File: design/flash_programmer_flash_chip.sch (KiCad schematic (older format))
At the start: 7 parts, among them U401 GLS27SF010

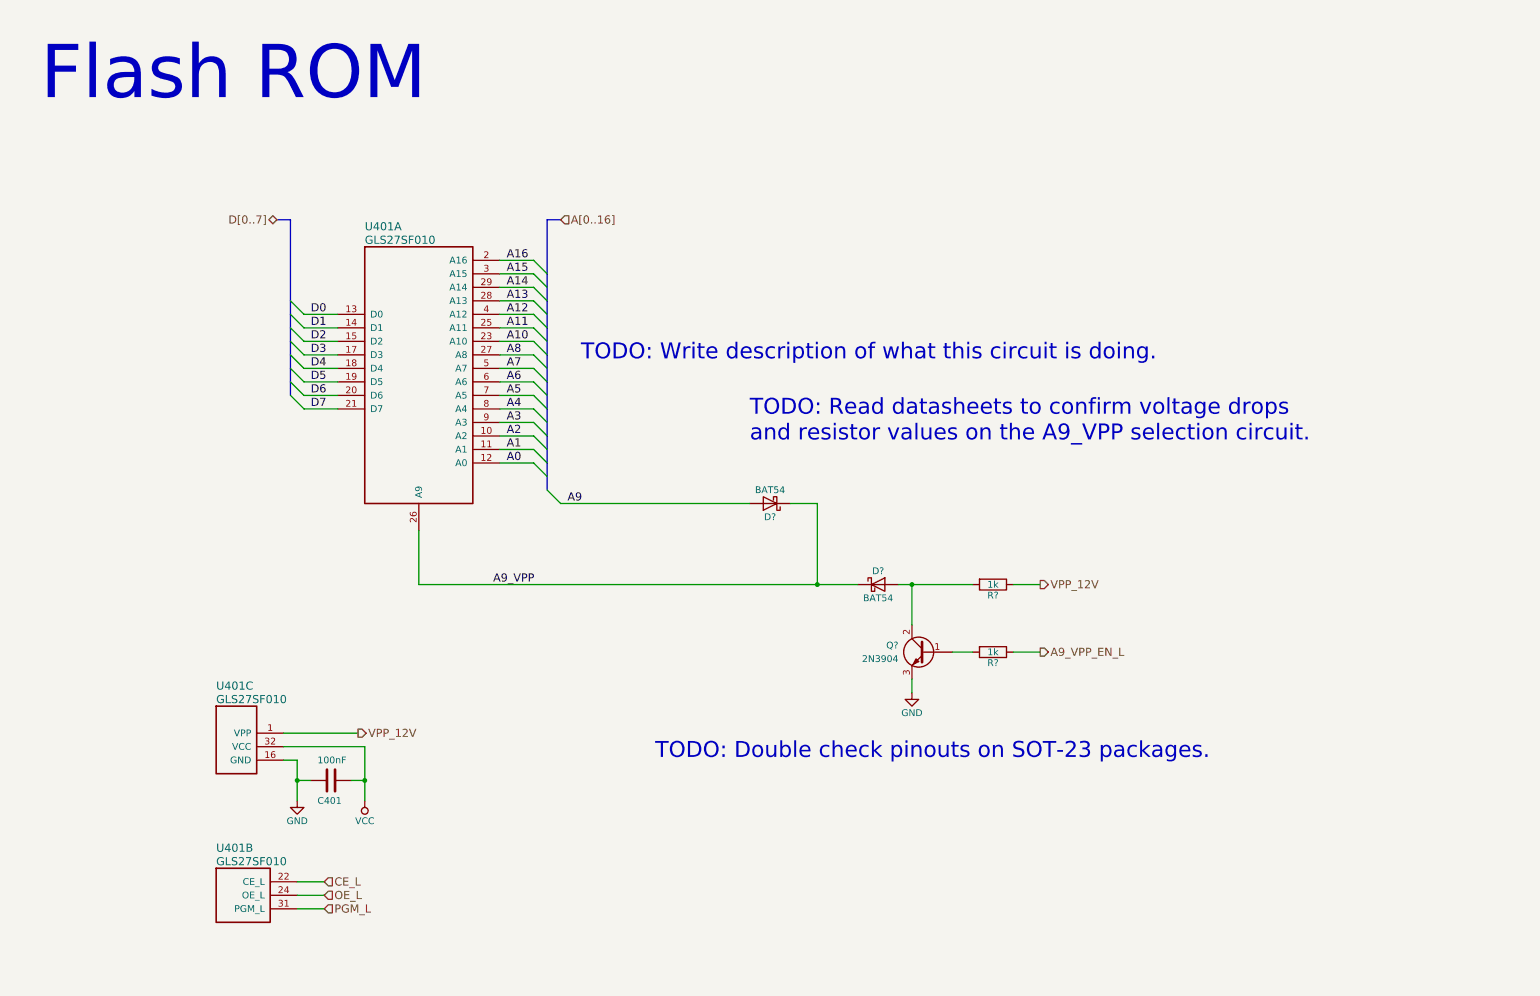
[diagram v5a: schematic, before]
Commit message: More schematic clean up
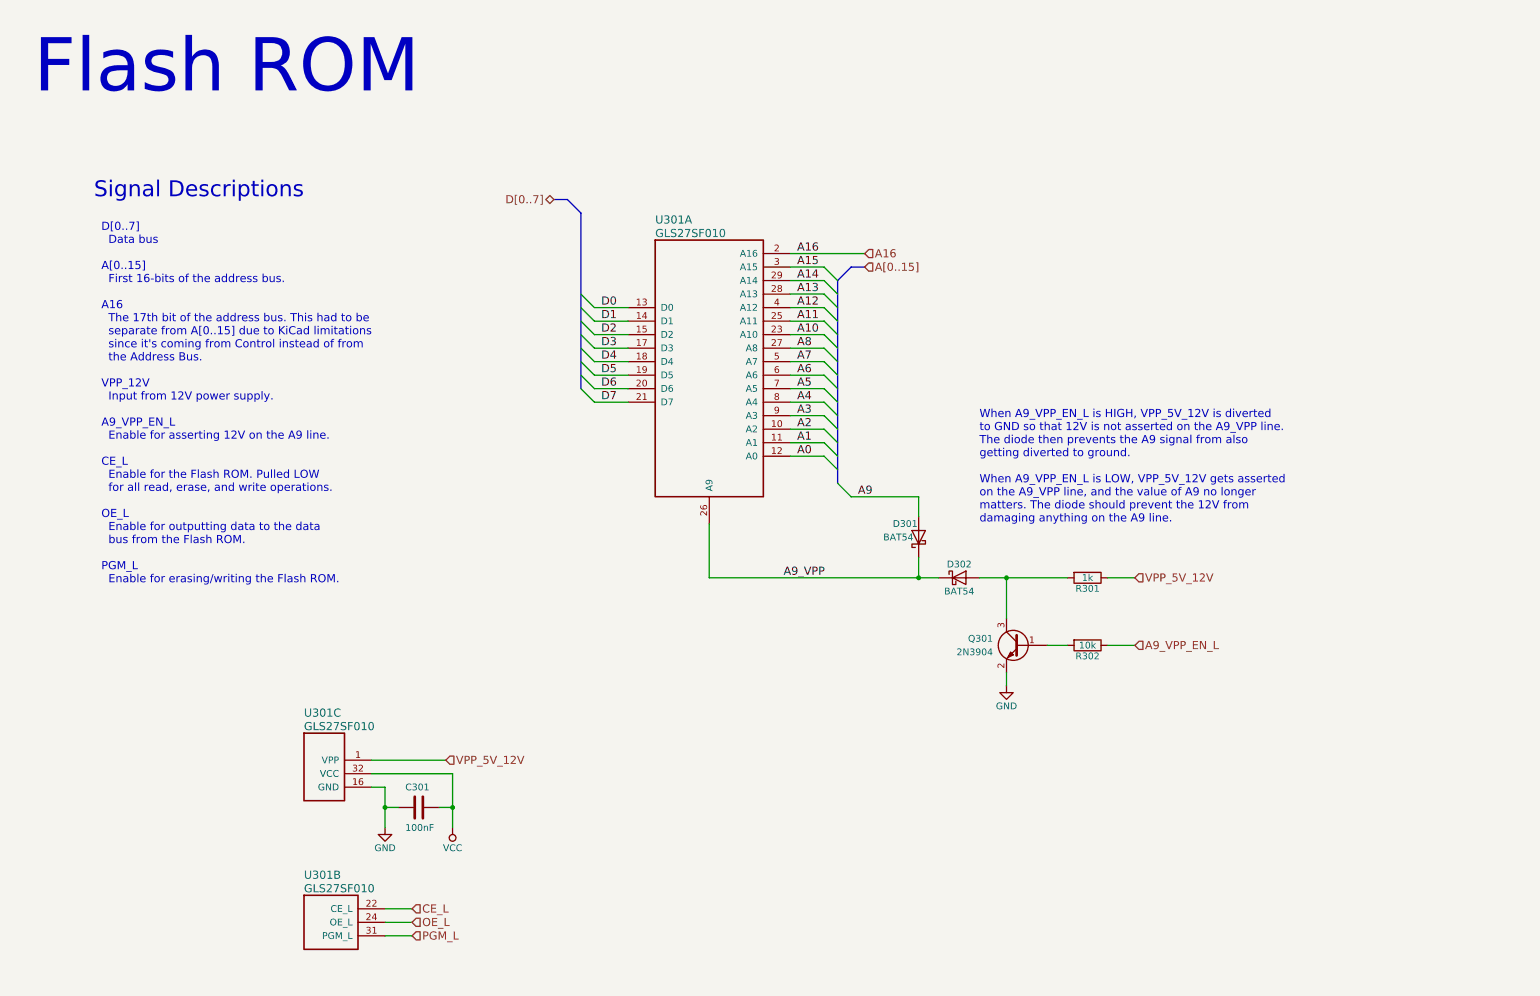
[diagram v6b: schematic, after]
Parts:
- removed Q?: 2N3904, symbol Q_NPN_BCE
- added Q301: 2N3904, TO_SOT_Packages_SMD:SOT-23_Handsoldering, symbol Q_NPN_BEC
- C301: renamed from C401; footprint Resistors_SMD:R_0805_HandSoldering -> Resistors_SMD:R_0603_HandSoldering
- D301, D302: renamed from D?; footprint (none) -> Diodes_SMD:D_SOT-23_ANK
- R301: renamed from R?; footprint (none) -> Resistors_SMD:R_0603_HandSoldering
- R302: renamed from R?; value 1k -> 10k; footprint (none) -> Resistors_SMD:R_0603_HandSoldering
- renumbered U401 to U301
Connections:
- net GND: now also Q301.2 (E)
- net at R302.2: now also Q301.1 (B)
- net at D302.2 (A), R301.2: now also Q301.3 (C)
- net VPP_12V renamed VPP_5V_12V
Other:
- note added: "D[0..7]\n Data bus\n\nA[0..15]\n First 16-bits of the address bus.\n\nA16\n The 17th bit of the address bus. This had to be\n separate from A[0..15] due to KiCad limitations\n since it's coming from Control instead of from\n the Address Bus.\n\nVPP_12V\n Input from 12V power supply.\n\nA9_VPP_EN_L\n Enable for asserting 12V on the A9 line.\n\nCE_L\n Enable for the Flash ROM. Pulled LOW\n for all 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"
- note added: "Signal Descriptions"
- note added: "When A9_VPP_EN_L is HIGH, VPP_5V_12V is diverted\nto GND so that 12V is not asserted on the A9_VPP line.\nThe diode then prevents the A9 signal from also\ngetting diverted to ground.\n\nWhen A9_VPP_EN_L is LOW, VPP_5V_12V gets asserted\non the A9_VPP line, and the value of A9 no longer\nmatters. The diode should prevent the 12V from\ndamaging anything on the A9 line."
- note removed: "TODO: Double check pinouts on SOT-23 packages."
- note removed: "TODO: Read datasheets to confirm voltage drops\nand resistor values on the A9_VPP selection circuit."
- note removed: "TODO: Write description of what this circuit is doing."
- moved on the sheet: C301, D301, D302, R301, R302, U301A, U301B, U301C

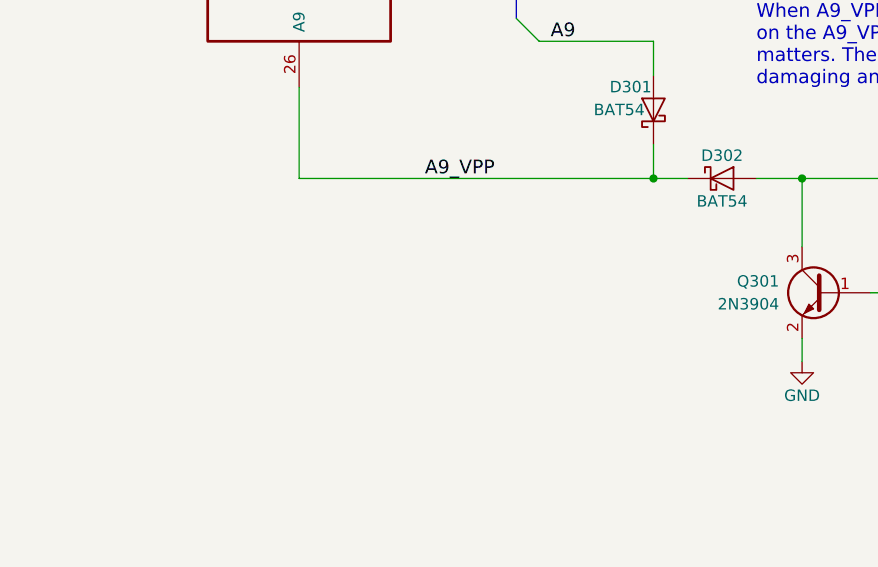
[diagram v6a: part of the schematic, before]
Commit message: Apply license to schematic files
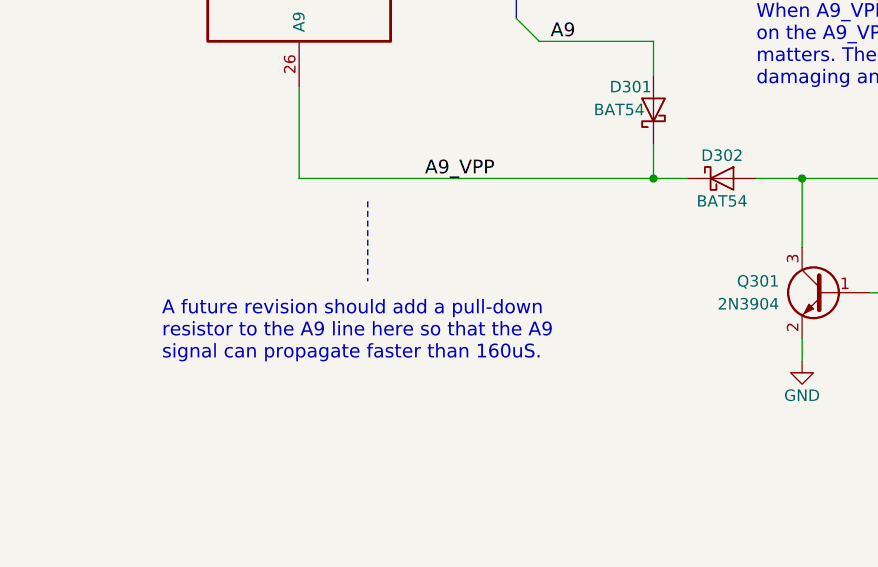
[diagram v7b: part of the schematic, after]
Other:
- note added: "A future revision should add a pull-down\nresistor to the A9 line here so that the A9\nsignal can propagate faster than 160uS."
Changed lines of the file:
@@
 Date "2017-03-11"
 Rev "5"
-Comp "John DiSanti"
+Comp "Copyright 2017 John DiSanti"
 Comment1 ""
 Comment2 ""
@@
 	-1   0    0    -1
 $EndComp
+Wire Notes Line
+	5900 4750 5900 5100
+Text Notes 5000 5450 0    60   ~ 0
+A future revision should add a pull-down\nresistor to the A9 line here so that the A9\nsignal can propagate faster than 160uS.
 $EndSCHEMATC
